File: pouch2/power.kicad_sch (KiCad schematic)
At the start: 55 parts, among them J501 Conn_01x02_Male, J502 Conn_01x02_Male, J503 Conn_01x02_Male, J504 Conn_01x02_Male, Q501 AO3401A, Q502 AO3401A, Q503 AO3401A, Q504 AO3401A, SW501 SW_SPDT

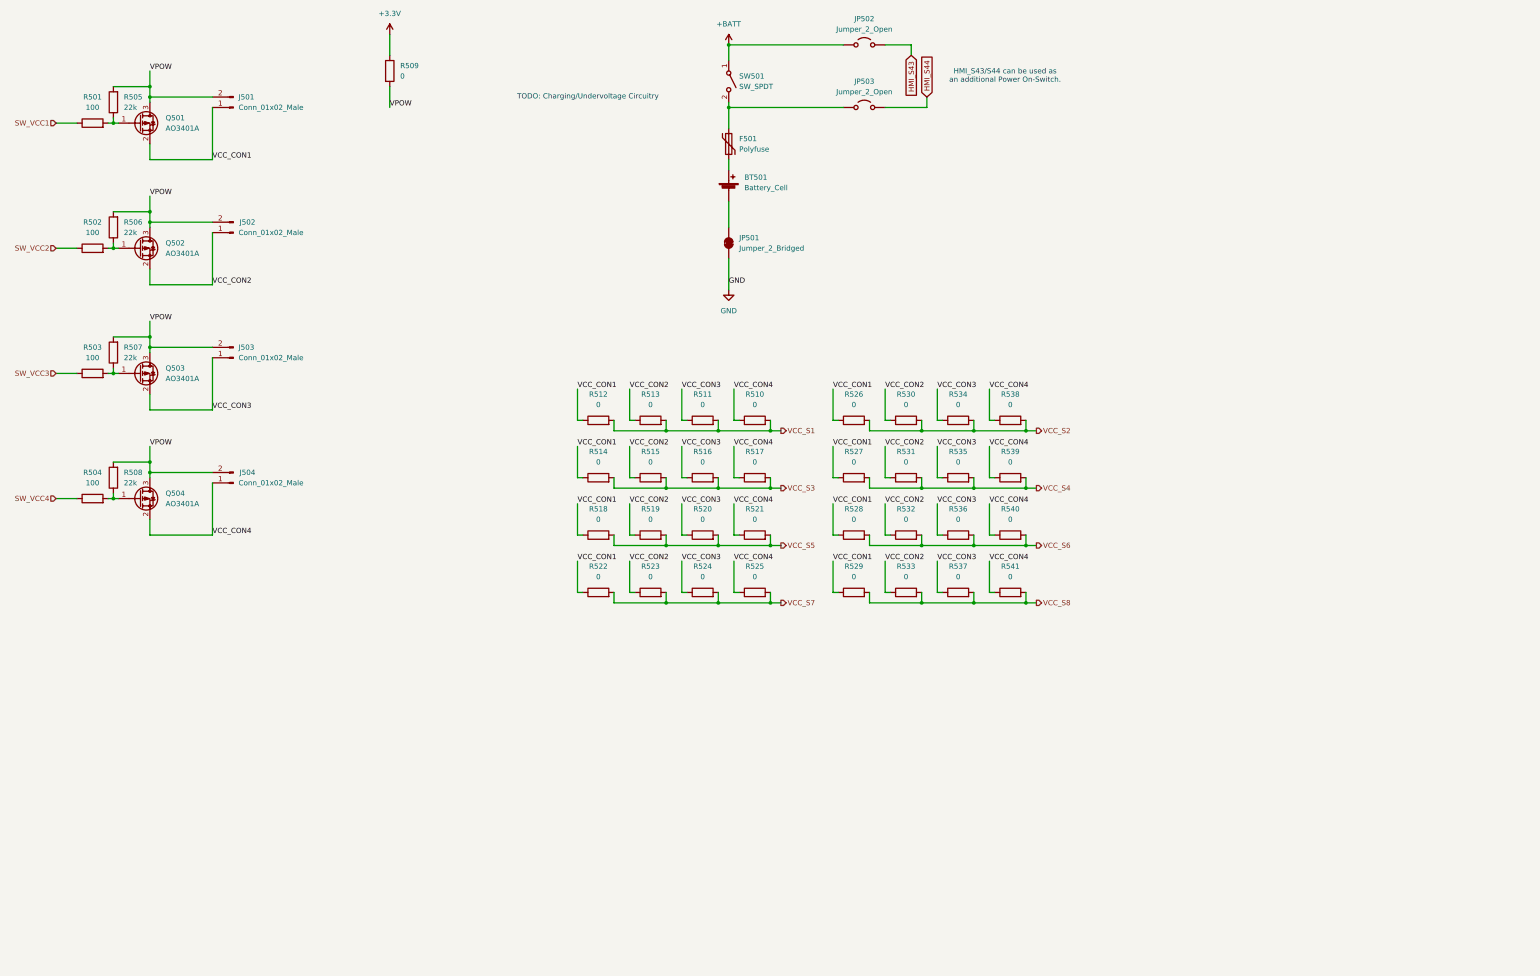
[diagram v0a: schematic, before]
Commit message: updated power routing
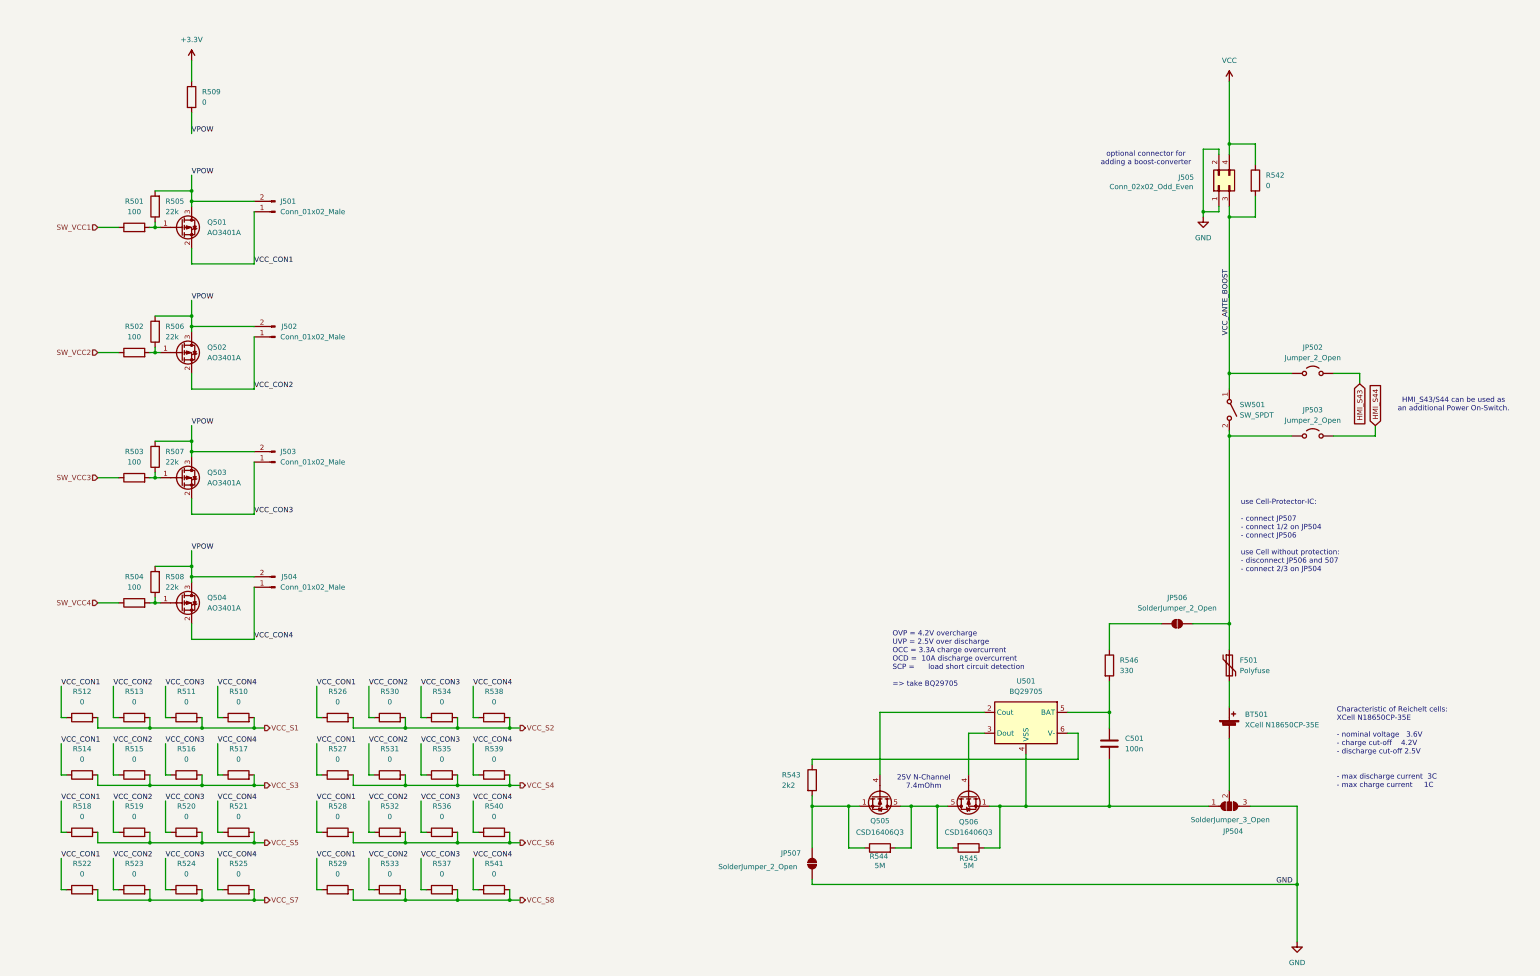
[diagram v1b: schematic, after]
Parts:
- removed JP501: Jumper_2_Bridged, Jumper:SolderJumper-2_P1.3mm_Bridged2Bar_Pad1.0x1.5mm, symbol Jumper:SolderJumper_2_Bridged
- added C501: 100n, Capacitor_SMD:C_0805_2012Metric, symbol Device:C
- added J505: Conn_02x02_Odd_Even, Connector_PinHeader_2.54mm:PinHeader_1x04_P2.54mm_Vertical, symbol Connector_Generic:Conn_02x02_Odd_Even
- added JP504: SolderJumper_3_Open, Jumper:SolderJumper-3_P2.0mm_Open_TrianglePad1.0x1.5mm_NumberLabels, symbol Jumper:SolderJumper_3_Open
- added JP506, JP507: SolderJumper_2_Open, Jumper:SolderJumper-2_P1.3mm_Open_TrianglePad1.0x1.5mm, symbol Jumper:SolderJumper_2_Open
- added Q505, Q506: CSD16406Q3, Package_SON:VSON-8-1EP_3x3mm_P0.65mm_EP1.65x2.4mm, symbol Transistor_FET:CSD16407Q5
- added R542: 0, Resistor_SMD:R_0805_2012Metric, symbol Device:R
- added R543: 2k2, Resistor_SMD:R_0805_2012Metric, symbol Device:R
- added R544, R545: 5M, Resistor_SMD:R_0805_2012Metric, symbol Device:R
- added R546: 330, Resistor_SMD:R_0805_2012Metric, symbol Device:R
- added U501: BQ29705, Package_SON:WSON-6_1.5x1.5mm_P0.5mm, symbol Battery_Management:BQ297xy
- BT501: value Battery_Cell -> XCell N18650CP-35E
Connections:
- net GND: now also J505.1 (Pin_1), J505.2 (Pin_2), JP504.3 (B), JP507.1 (A)
- net at F501.1, JP503.1 (A), SW501.2 (B): now also JP506.1 (A)
- net at BT501.2 (-): now also JP504.2 (C)
- net +BATT renamed VCC_ANTE_BOOST
- net VCC_ANTE_BOOST: now also J505.3 (Pin_3), R542.2
- new net: JP507.2 (B), Q505.1 (S), Q505.2 (S), Q505.3 (S), R543.2, R544.1
- new net: Q505.4 (G), U501.2 (Cout)
- new net: Q505.5 (D), Q506.5 (D), R544.2, R545.2
- new net: C501.1, R546.2, U501.5 (BAT)
- new net: C501.2, JP504.1 (A), Q506.1 (S), Q506.2 (S), Q506.3 (S), R545.1, U501.4 (VSS)
- new net: Q506.4 (G), U501.3 (Dout)
- new net: R543.1, U501.6 (V-)
- new net: JP506.2 (B), R546.1
- new net VCC: J505.4 (Pin_4), R542.1
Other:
- note added: "25V N-Channel 7.4mOhm"
- note added: "Characteristic of Reichelt cells: XCell N18650CP-35E - nominal voltage 3.6V - charge cut-off 4.2V - discharge cut-off 2.5V - max discharge current 3C - max charge current 1C"
- note added: "OVP = 4.2V overcharge UVP = 2.5V over discharge OCC = 3.3A charge overcurrent OCD = 10A discharge overcurrent SCP = load short circuit detection => take BQ29705"
- note added: "optional connector for adding a boost-converter"
- note added: "use Cell-Protector-IC: - connect JP507 - connect 1/2 on JP504 - connect JP506 use Cell without protection: - disconnect JP506 and 507 - connect 2/3 on JP504"
- note removed: "TODO: Charging/Undervoltage Circuitry"
- moved on the sheet: BT501, F501, J501, J502, J503, J504, JP502, JP503, Q501, Q502, Q503, Q504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

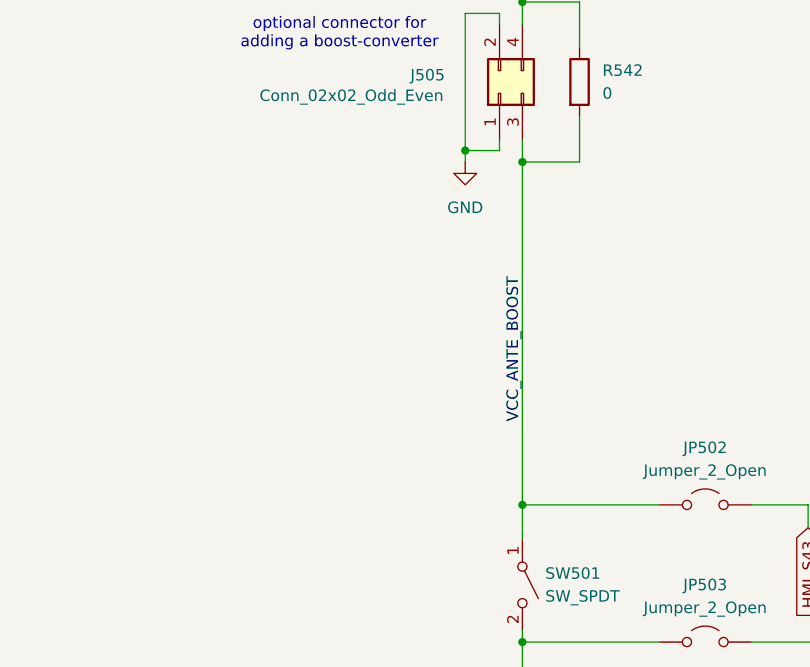
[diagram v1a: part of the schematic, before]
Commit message: added VCC-battery measurement line
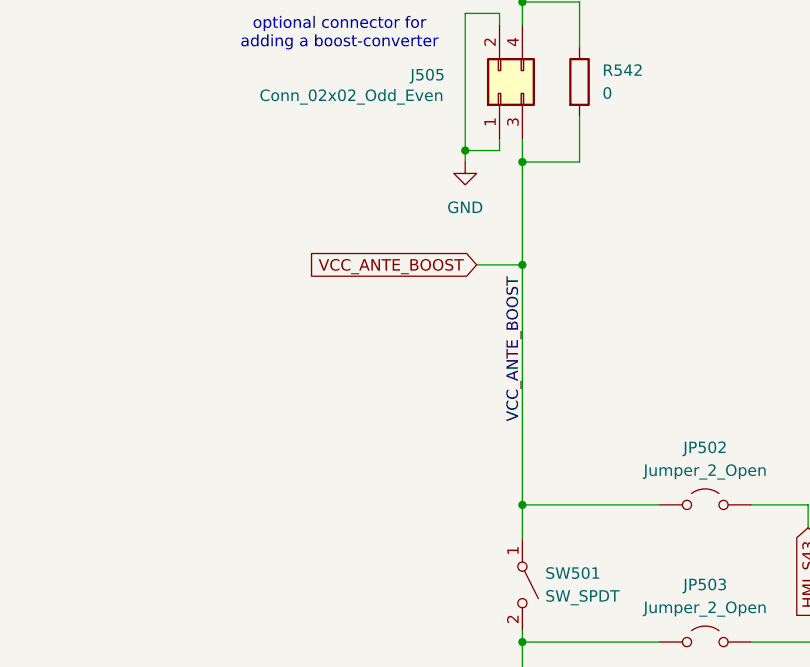
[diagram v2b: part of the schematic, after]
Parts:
- C501: MPN_Eurocircuit (none) -> GPC0805104
- Q501, Q502, Q503, Q504: MPN_Eurocircuit (none) -> AO3401A
- Q505, Q506: MPN_Eurocircuit (none) -> CSD16406Q3
- R501, R502, R503, R504: LCSC (none) -> C17408; MPN_Eurocircuit (none) -> GPR0805100R
- R505, R506, R507, R508: LCSC (none) -> C17560; MPN_Eurocircuit (none) -> GPR080522K
- R509, R510, R511, R512, R513, R514, R515, R516, R517, R518, R519, R520, R521, R522, R523, R524, R525, R526, R527, R528, R529, R530, R531, R532, R533, R534, R535, R536, R537, R538, R539, R540, R541, R542: LCSC (none) -> C17477; MPN_Eurocircuit (none) -> GPR08050R
- R543: LCSC (none) -> C17520; MPN_Eurocircuit (none) -> GPR08052K2
- R544, R545: LCSC (none) -> C2933370; MPN_Eurocircuit (none) -> GPR08055M1
- R546: LCSC (none) -> C17630; MPN_Eurocircuit (none) -> GPR0805330R
- U501: MPN_Eurocircuit (none) -> BQ29705DSER

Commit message: rev1
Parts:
- BT501, J501, J502, J503, J504, J505, SW501: OrderStatus (none) -> manual
- C501, R501, R502, R503, R504, R505, R506, R507, R508, R509, R510, R511, R512, R513, R514, R515, R516, R517, R518, R519, R520, R521, R522, R523, R524, R525, R526, R527, R528, R529, R530, R531, R532, R533, R534, R535, R536, R537, R538, R539, R540, R541, R542, R543, R544, R545, R546: OrderStatus (none) -> assembly
- F501, Q501, Q502, Q503, Q504, Q505, Q506, U501: OrderStatus (none) -> order
- JP502, JP503, JP504, JP506, JP507: OrderStatus (none) -> dnp
